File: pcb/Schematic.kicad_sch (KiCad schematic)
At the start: 19 parts, among them SW1 SW_Push, SW2 SW_Push, SW3 SW_Push, SW4 SW_Push, SW5 SW_Push, SW6 SW_Push, SW7 RotaryEncoder_Switch, SW8 SW_Push, U1 XIAO-RP2040-DIP

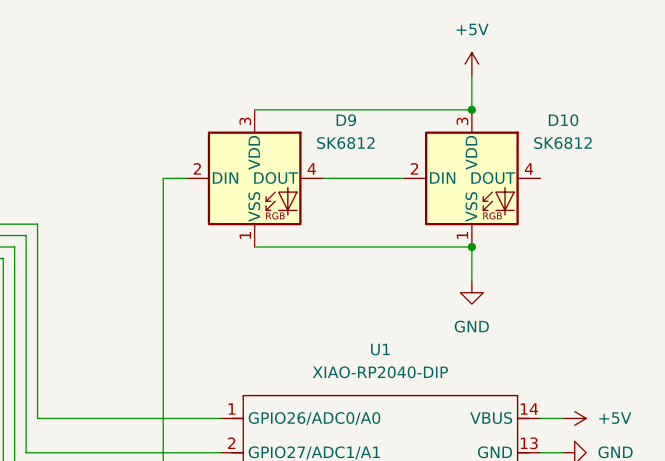
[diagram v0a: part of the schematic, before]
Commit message: new leds
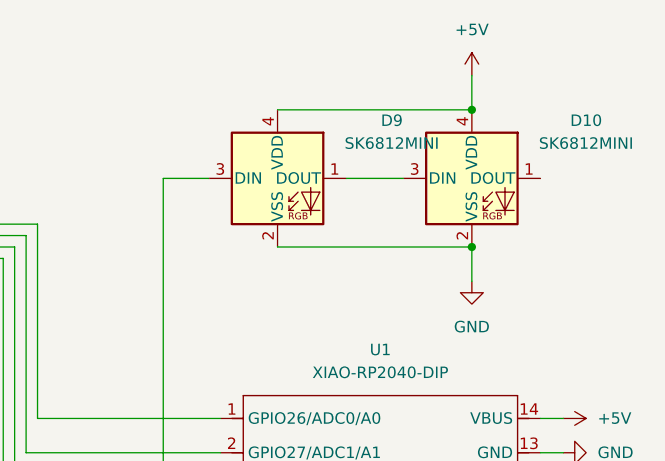
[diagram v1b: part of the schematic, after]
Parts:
- removed D10, D9: SK6812, LED_SMD:LED_SK6812MINI_PLCC4_3.5x3.5mm_P1.75mm, symbol LED:SK6812
- added D10, D9: SK6812MINI, Meine_Bauteile:MX_SK6812MINI-E_REV, symbol LED:SK6812MINI
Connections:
- net +5V: now also D10.4 (VDD), D9.4 (VDD)
- net GND: now also D10.2 (VSS), D9.2 (VSS)
- net at U1.7 (GPIO0/TX): now also D9.3 (DIN)
- new net: D10.3 (DIN), D9.1 (DOUT)
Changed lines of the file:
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@@
+	)
+	(junction
+		(at 128.27 25.4)
+		(diameter 0)
+		(color 0 0 0 0)
 	)
 	(junction
@@
 	)
 	(junction
-		(at 128.27 25.4)
-		(diameter 0)
-		(color 0 0 0 0)
-	)
-	(junction
 		(at 22.86 52.07)
 		(diameter 0)
@@
 	(wire
 		(pts
-			(xy 96.52 33.02) (xy 93.98 33.02)
+			(xy 93.98 33.02) (xy 99.06 33.02)
 		)
 		(stroke
@@
 	(wire
 		(pts
+			(xy 106.68 25.4) (xy 128.27 25.4)
+		)
+		(stroke
+			(width 0)
+			(type default)
+		)
+	)
+	(wire
+		(pts
 			(xy 22.86 41.91) (xy 76.2 41.91)
 		)
@@
 	(wire
 		(pts
+			(xy 114.3 33.02) (xy 120.65 33.02)
+		)
+		(stroke
+			(width 0)
+			(type default)
+		)
+	)
+	(wire
+		(pts
 			(xy 43.18 115.57) (xy 146.05 115.57)
 		)
@@
 	(wire
 		(pts
-			(xy 111.76 33.02) (xy 120.65 33.02)
-		)
-		(stroke
-			(width 0)
-			(type default)
-		)
-	)
-	(wire
-		(pts
-			(xy 104.14 25.4) (xy 128.27 25.4)
-		)
-		(stroke
-			(width 0)
-			(type default)
-		)
-	)
-	(wire
-		(pts
 			(xy 54.61 86.36) (xy 22.86 86.36)
 		)
@@
 	(wire
 		(pts
+			(xy 106.68 40.64) (xy 128.27 40.64)
+		)
+		(stroke
+			(width 0)
+			(type default)
+		)
+	)
+	(wire
+		(pts
 			(xy 53.34 66.04) (xy 22.86 66.04)
 		)
@@
 		(pts
 			(xy 20.32 39.37) (xy 78.74 39.37)
-		)
-		(stroke
-			(width 0)
-			(type default)
-		)
-	)
-	(wire
-		(pts
-			(xy 104.14 40.64) (xy 128.27 40.64)
 		)
 		(stroke
@@
 			)
 		)
-		(property "Datasheet" ""
+		(property "Datasheet" "https://wiki.seeedstudio.com/XIAO-RP2040/"
 			(at 104.14 54.61 0)
 			(effects
@@
 			)
 		)
-		(property "Datasheet" "~"
+		(property "Datasheet" "https://cdn.sparkfun.com/datasheets/Components/Switches/MX%20Series.pdf"
 			(at 58.42 72.39 0)
 			(effects
@@
 			)
 		)
-		(property "Datasheet" "~"
+		(property "Datasheet" "https://cdn.sparkfun.com/datasheets/Components/Switches/MX%20Series.pdf"
 			(at 58.42 50.8 0)
 			(effects
@@
 			)
 		)
-		(property "Datasheet" "~"
+		(property "Datasheet" "https://cdn.sparkfun.com/datasheets/Components/Switches/MX%20Series.pdf"
 			(at 58.42 60.96 0)
 			(effects
@@
 			)
 		)
-		(property "Datasheet" "~"
+		(property "Datasheet" "https://cdn.sparkfun.com/datasheets/Components/Switches/MX%20Series.pdf"
 			(at 27.94 71.12 0)
 			(effects
@@
 	)
 	(symbol
-		(lib_id "LED:SK6812")
-		(at 128.27 33.02 0)
-		(unit 1)
-		(exclude_from_sim no)
-		(in_bom yes)
-		(on_board yes)
-		(dnp no)
-		(fields_autoplaced yes)
-		(property "Reference" "D10"
-			(at 138.43 26.5998 0)
-			(effects
-				(font
-					(size 1.27 1.27)
-				)
-			)
-		)
-		(property "Value" "SK6812"
-			(at 138.43 29.1398 0)
-			(effects
-				(font
-					(size 1.27 1.27)
-				)
-			)
-		)
-		(property "Footprint" "LED_SMD:LED_SK6812MINI_PLCC4_3.5x3.5mm_P1.75mm"
-			(at 129.54 40.64 0)
-			(effects
-				(font
-					(size 1.27 1.27)
-				)
-				(justify left top)
-				(hide yes)
-			)
-		)
-		(property "Datasheet" "https://cdn-shop.adafruit.com/product-files/1138/SK6812+LED+datasheet+.pdf"
-			(at 130.81 42.545 0)
-			(effects
-				(font
-					(size 1.27 1.27)
-				)
-				(justify left top)
-				(hide yes)
-			)
-		)
-		(property "Description" "RGB LED with integrated controller"
-			(at 128.27 33.02 0)
-			(effects
-				(font
-					(size 1.27 1.27)
-				)
-				(hide yes)
-			)
-		)
-		(pin "3"
-		)
-		(pin "4"
-		)
-		(pin "1"
-		)
-		(pin "2"
-		)
-		(instances
-			(project ""
-				(path "/822432d2-0699-4371-a661-158873cfbbb0"
-					(reference "D10")
-					(unit 1)
-				)
-			)
-		)
-	)
-	(symbol
 		(lib_id "Diode:1N4148")
 		(at 69.85 66.04 180)
@@
 			)
 		)
-		(property "Datasheet" "~"
+		(property "Datasheet" "https://cdn.sparkfun.com/datasheets/Components/Switches/MX%20Series.pdf"
 			(at 27.94 58.42 0)
 			(effects
@@
 			)
 		)
-		(property "Datasheet" "~"
+		(property "Datasheet" "https://cdn.sparkfun.com/datasheets/Components/Switches/MX%20Series.pdf"
 			(at 27.94 46.99 0)
 			(effects
@@
 				(path "/822432d2-0699-4371-a661-158873cfbbb0"
 					(reference "SW1")
-					(unit 1)
-				)
-			)
-		)
-	)
-	(symbol
-		(lib_id "LED:SK6812")
-		(at 104.14 33.02 0)
-		(unit 1)
-		(exclude_from_sim no)
-		(in_bom yes)
-		(on_board yes)
-		(dnp no)
-		(fields_autoplaced yes)
-		(property "Reference" "D9"
-			(at 114.3 26.5998 0)
-			(effects
-				(font
-					(size 1.27 1.27)
-				)
-			)
-		)
-		(property "Value" "SK6812"
-			(at 114.3 29.1398 0)
-			(effects
-				(font
-					(size 1.27 1.27)
-				)
-			)
-		)
-		(property "Footprint" "LED_SMD:LED_SK6812MINI_PLCC4_3.5x3.5mm_P1.75mm"
-			(at 105.41 40.64 0)
-			(effects
-				(font
-					(size 1.27 1.27)
-				)
-				(justify left top)
-				(hide yes)
-			)
-		)
-		(property "Datasheet" "https://cdn-shop.adafruit.com/product-files/1138/SK6812+LED+datasheet+.pdf"
-			(at 106.68 42.545 0)
-			(effects
-				(font
-					(size 1.27 1.27)
-				)
-				(justify left top)
-				(hide yes)
-			)
-		)
-		(property "Description" "RGB LED with integrated controller"
-			(at 104.14 33.02 0)
-			(effects
-				(font
-					(size 1.27 1.27)
-				)
-				(hide yes)
-			)
-		)
-		(pin "2"
-		)
-		(pin "1"
-		)
-		(pin "4"
-		)
-		(pin "3"
-		)
-		(instances
-			(project ""
-				(path "/822432d2-0699-4371-a661-158873cfbbb0"
-					(reference "D9")
 					(unit 1)
 				)
@@
 			)
 		)
-		(property "Datasheet" "~"
+		(property "Datasheet" "https://cdn.sparkfun.com/datasheets/Components/Switches/MX%20Series.pdf"
 			(at 27.94 83.82 0)
 			(effects
@@
 	)
 	(symbol
+		(lib_id "LED:SK6812MINI")
+		(at 106.68 33.02 0)
+		(unit 1)
+		(exclude_from_sim no)
+		(in_bom yes)
+		(on_board yes)
+		(dnp no)
+		(fields_autoplaced yes)
+		(property "Reference" "D9"
+			(at 119.38 26.5998 0)
+			(effects
+				(font
+					(size 1.27 1.27)
+				)
+			)
+		)
+		(property "Value" "SK6812MINI"
+			(at 119.38 29.1398 0)
+			(effects
+				(font
+					(size 1.27 1.27)
+				)
+			)
+		)
+		(property "Footprint" "Meine_Bauteile:MX_SK6812MINI-E_REV"
+			(at 107.95 40.64 0)
+			(effects
+				(font
+					(size 1.27 1.27)
+				)
+				(justify left top)
+				(hide yes)
+			)
+		)
+		(property "Datasheet" "https://cdn-shop.adafruit.com/product-files/2686/SK6812MINI_REV.01-1-2.pdf"
+			(at 109.22 42.545 0)
+			(effects
+				(font
+					(size 1.27 1.27)
+				)
+				(justify left top)
+				(hide yes)
+			)
+		)
+		(property "Description" "RGB LED with integrated controller"
+			(at 106.68 33.02 0)
+			(effects
+				(font
+					(size 1.27 1.27)
+				)
+				(hide yes)
+			)
+		)
+		(pin "4"
+		)
+		(pin "1"
+		)
+		(pin "3"
+		)
+		(pin "2"
+		)
+		(instances
+			(project ""
+				(path "/822432d2-0699-4371-a661-158873cfbbb0"
+					(reference "D9")
+					(unit 1)
+				)
+			)
+		)
+	)
+	(symbol
 		(lib_id "Diode:1N4148")
 		(at 39.37 88.9 180)
@@
 					(unit 1)
 				)
+			)
+		)
+	)
+	(symbol
+		(lib_id "LED:SK6812MINI")
+		(at 128.27 33.02 0)
+		(unit 1)
+		(exclude_from_sim no)
+		(in_bom yes)
+		(on_board yes)
+		(dnp no)
+		(fields_autoplaced yes)
+		(property "Reference" "D10"
+			(at 140.97 26.5998 0)
+			(effects
+				(font
+					(size 1.27 1.27)
+				)
+			)
+		)
+		(property "Value" "SK6812MINI"
+			(at 140.97 29.1398 0)
+			(effects
+				(font
+					(size 1.27 1.27)
+				)
+			)
+		)
+		(property "Footprint" "Meine_Bauteile:MX_SK6812MINI-E_REV"
+			(at 129.54 40.64 0)
+			(effects
+				(font
+					(size 1.27 1.27)
+				)
+				(justify left top)
+				(hide yes)
+			)
+		)
+		(property "Datasheet" "https://cdn-shop.adafruit.com/product-files/2686/SK6812MINI_REV.01-1-2.pdf"
+			(at 130.81 42.545 0)
+			(effects
+				(font
+					(size 1.27 1.27)
+				)
+				(justify left top)
+				(hide yes)
+			)
+		)
+		(property "Description" "RGB LED with integrated controller"
+			(at 128.27 33.02 0)
+			(effects
+				(font
+					(size 1.27 1.27)
+				)
+				(hide yes)
+			)
+		)
+		(pin "3"
+		)
+		(pin "2"
+		)
+		(pin "1"
+		)
+		(pin "4"
+		)
+		(instances
+			(project ""
+				(path "/822432d2-0699-4371-a661-158873cfbbb0"
+					(reference "D10")
+					(unit 1)
+				)
